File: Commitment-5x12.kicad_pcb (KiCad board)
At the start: 2 copper layers, 234.4 x 118.4 mm, 95 parts, among them J1 Conn_01x13, J2 Conn_01x13, J3 Conn_01x03, J4 Conn_01x04, J5 Conn_01x04, SW1 OS102011MS2QN1, SW2 RotaryEncoder

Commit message: working toward rev 1
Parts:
- added M1: ~, lizard_libs:MX_2U_Stabilizer_Mount, F.Cu at (159.4, 138.4)
- added M2: ~, lizard_libs:MX_2U_Stabilizer_Mount, F.Cu at (121.3, 138.4)
- MX1, MX10, MX11, MX12, MX13, MX14, MX15, MX16, MX17, MX18, MX19, MX2, MX20, MX21, MX22, MX23, MX24, MX26, MX27, MX28, MX29, MX3, MX31, MX32, MX33, MX34, MX36, MX37, MX38, MX39, MX4, MX41, MX42, MX43, MX44, MX45, MX46, MX47, MX48, MX49, MX5, MX50, MX51, MX52, MX53, MX54, MX55, MX56, MX57, MX58, MX59, MX6, MX60, MX7, MX8, MX9: footprint lizard_libs:SW_Cherry_MX_1.00u_PCB -> lizard_libs:hotswap_keyswitch_reflow
- MX25, MX40: footprint lizard_libs:SW_Cherry_MX_2.00u_PCB -> lizard_libs:hotswap_keyswitch_reflow
- moved D1 17.7 mm to (66.0, 63.5)
- moved D13 17.7 mm to (66.0, 120.7)
- moved D9 17.6 mm to (66.0, 101.6)
- moved D3 17.6 mm to (180.3, 63.5)
- moved D17 17.6 mm to (66.0, 139.7)
- moved D5 17.6 mm to (66.0, 82.5)
- moved D2 17.6 mm to (123.2, 63.5)
- moved D15 17.5 mm to (180.3, 120.7)
- moved D14 17.5 mm to (123.2, 120.7)
- moved D11 17.5 mm to (180.3, 101.6)
- moved D10 17.5 mm to (123.2, 101.6)
- moved D7 17.5 mm to (180.3, 82.5)
- moved D6 17.5 mm to (123.2, 82.5)
- moved D19 11.3 mm to (173.7, 135.6)
- moved D18 7.04 mm to (112.1, 135.6)
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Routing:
- net COL 12: track 412.0 -> 334.2 mm, vias 1 -> 8
- net COL 3: track 207.3 -> 148.2 mm, vias 0 -> 7
- net COL 11: track 347.0 -> 288.6 mm, vias 1 -> 7
- net COL 10: track 313.3 -> 255.3 mm, vias 1 -> 7
- net GND: track 100.0 -> 50.7 mm, vias 100 -> 102
- net /BAT +: track 353.9 -> 307.0 mm, vias 8 -> 3
- net COL 8: track 271.3 -> 233.3 mm, vias 1 -> 7
- net COL 4: track 185.5 -> 149.2 mm, vias 1 -> 7
- net COL 9: track 288.8 -> 253.6 mm, vias 2 -> 7
- net COL 5: track 223.3 -> 188.5 mm, vias 1 -> 7
- net ROW 4: track 255.4 -> 272.2 mm
- net ROW 1: track 213.1 -> 228.7 mm
- net Net-(D13A-A): track 6.15 -> 20.9 mm
- net Net-(D1A-A): track 6.19 -> 20.6 mm
- net Net-(D15A-A): track 7.35 -> 20.9 mm
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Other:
- outline, holes or cut-outs redrawn

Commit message: working toward rev 1
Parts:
- moved BAT1 8.89 mm to (190.5, 35.6)
- moved G*** 8.89 mm to (190.5, 35.6)
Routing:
- net Net-(BAT1-+): track 113.7 -> 104.3 mm
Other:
- outline, holes or cut-outs redrawn
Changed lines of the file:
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@@
 		(pad_to_mask_clearance 0)
 		(allow_soldermask_bridges_in_footprints no)
-		(grid_origin 35.56 62.23)
+		(grid_origin 38.1 57.15)
 		(pcbplotparams
 			(layerselection 0x00010fc_ffffffff)
@@
 		(tags "Cherry MX keyswitch 2.00u PCB")
 		(property "Reference" "M1"
-			(at -2.54 -2.794 360)
+			(at -2.54 -2.794 0)
 			(layer "F.SilkS")
 			(hide yes)
@@
 		)
 		(property "Value" "~"
-			(at -2.54 12.954 360)
+			(at -2.54 12.954 0)
 			(layer "F.Fab")
 			(effects
@@
 		)
 		(fp_text user "${REFERENCE}"
-			(at -2.54 -2.794 360)
+			(at -2.54 -2.794 0)
 			(layer "F.Fab")
 			(effects
@@
 	(footprint "lizard_libs:Lizard Text Logo"
 		(layer "F.Cu")
-		(at 199.39 35.56)
+		(at 190.5 35.56)
 		(property "Reference" "G***"
 			(at 0 2.54 0)
@@
 		(tags "Cherry MX keyswitch 2.00u PCB")
 		(property "Reference" "M2"
-			(at -2.54 -2.794 360)
+			(at -2.54 -2.794 0)
 			(layer "F.SilkS")
 			(hide yes)
@@
 		)
 		(property "Value" "~"
-			(at -2.54 12.954 360)
+			(at -2.54 12.954 0)
 			(layer "F.Fab")
 			(effects
@@
 		)
 		(fp_text user "${REFERENCE}"
-			(at -2.54 -2.794 360)
+			(at -2.54 -2.794 0)
 			(layer "F.Fab")
 			(effects
@@
 	(footprint "lizard_libs:Keystone 1043 18650"
 		(layer "F.Cu")
-		(at 199.39 35.56 180)
+		(at 190.5 35.56 180)
 		(property "Reference" "BAT1"
 			(at 0 -2.54 180)
@@
 	)
 	(gr_arc
-		(start 159.766 26.2255)
-		(mid 160.230968 25.102968)
-		(end 161.3535 24.638)
+		(start 149.606 26.2255)
+		(mid 150.070968 25.102968)
+		(end 151.1935 24.638)
 		(stroke
 			(width 0.05)
@@
 	)
 	(gr_line
-		(start 159.766 26.2255)
-		(end 159.766 43.3705)
+		(start 149.606 26.2255)
+		(end 149.606 43.3705)
 		(stroke
 			(width 0.05)
@@
 	)
 	(gr_line
-		(start 158.1785 44.958)
+		(start 148.0185 44.958)
 		(end 81.3435 44.958)
 		(stroke
@@
 	)
 	(gr_arc
-		(start 159.766 43.3705)
-		(mid 159.301032 44.493032)
-		(end 158.1785 44.958)
+		(start 149.606 43.3705)
+		(mid 149.141032 44.493032)
+		(end 148.0185 44.958)
 		(stroke
 			(width 0.05)
@@
 	)
 	(gr_line
-		(start 161.3535 24.638)
+		(start 151.1935 24.638)
 		(end 255.7145 24.638)
 		(stroke
@@
 	)
 	(gr_text "+"
-		(at 172.466 35.433 180)
+		(at 163.576 35.433 180)
 		(layer "F.SilkS")
 		(effects
@@
 	)
 	(gr_text "-"
-		(at 227.711 35.433 180)
+		(at 218.821 35.433 180)
 		(layer "F.SilkS")
 		(effects
@@
 	)
 	(segment
-		(start 70.39 34.83)
-		(end 72.39 36.83)
-		(width 1.27)
-		(layer "F.Cu")
-		(net 1)
-	)
-	(segment
-		(start 163.322 44.45)
-		(end 163.322 35.6235)
+		(start 68.58 34.83)
+		(end 70.39 34.83)
 		(width 1.27)
 		(layer "F.Cu")
@@
 	(segment
 		(start 75.184 46.736)
-		(end 161.036 46.736)
+		(end 151.384 46.736)
 		(width 1.27)
 		(layer "F.Cu")
@@
 	)
 	(segment
-		(start 163.322 35.6235)
-		(end 163.2585 35.56)
+		(start 154.3685 43.7515)
+		(end 154.3685 35.56)
 		(width 1.27)
 		(layer "F.Cu")
@@
 	)
 	(segment
-		(start 68.58 34.83)
-		(end 70.39 34.83)
+		(start 70.39 34.83)
+		(end 72.39 36.83)
 		(width 1.27)
 		(layer "F.Cu")
@@
 	)
 	(segment
-		(start 161.036 46.736)
-		(end 163.322 44.45)
+		(start 151.384 46.736)
+		(end 154.3685 43.7515)
 		(width 1.27)
 		(layer "F.Cu")
@@
 		)
 	)
+	(group ""
+		(members "3122b99c-ad25-44f4-953b-640c3fc964a2" "711c629b-a350-407e-8104-c2bea098a2da"
+			"d03c237c-e164-42e6-be8a-686f8292c659"
+		)
+	)

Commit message: Update Commitment-5x12.kicad_pcb
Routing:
- net Net-(D21-A): track 54.6 -> 55.3 mm
- net GND: vias 102 -> 106
- net (no net): vias 0 -> 1
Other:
- board text added: "JLCJLCJLCJLC"

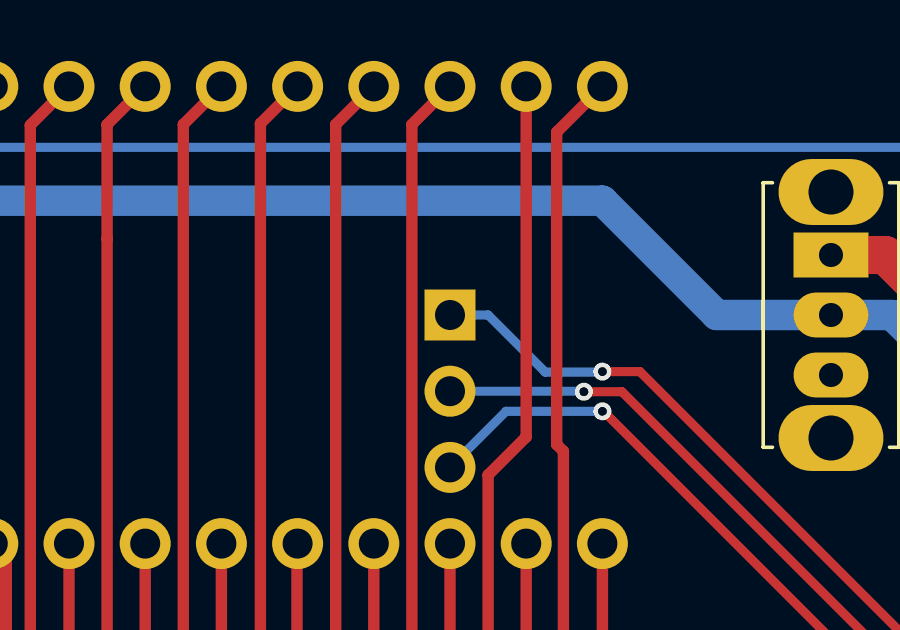
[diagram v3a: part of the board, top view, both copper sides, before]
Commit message: updated footprints to include 3D cad files
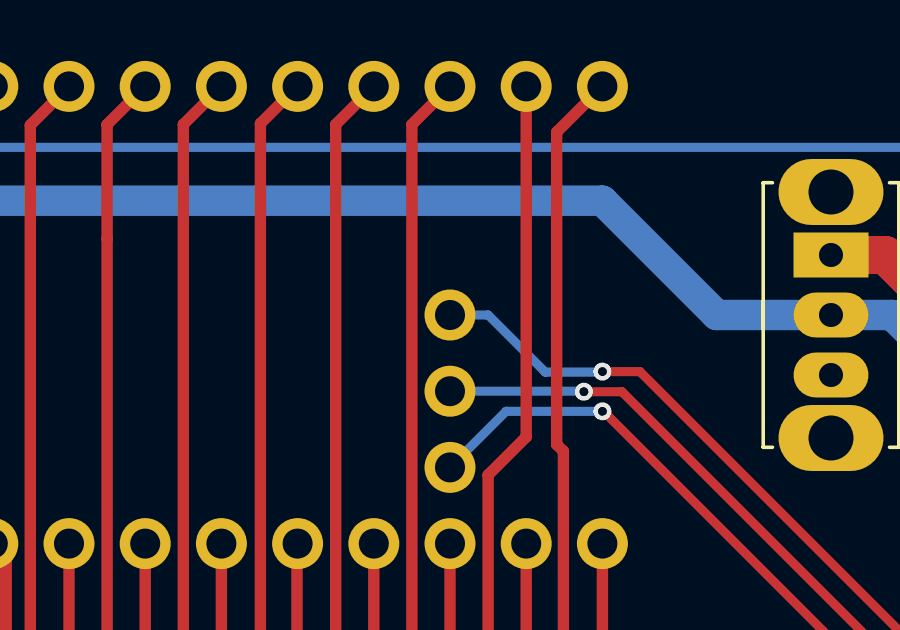
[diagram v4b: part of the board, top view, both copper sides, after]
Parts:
- J3: footprint lizard_libs:PinHeader_1x03_P2.54mm_Vertical -> lizard_libs:PinSocket_1x03_P2.54mm_Vertical
- MX1, MX10, MX11, MX12, MX13, MX14, MX15, MX16, MX17, MX18, MX19, MX2, MX20, MX21, MX22, MX23, MX24, MX25, MX26, MX27, MX28, MX29, MX3, MX31, MX32, MX33, MX34, MX36, MX37, MX38, MX39, MX4, MX40, MX41, MX42, MX43, MX44, MX45, MX46, MX47, MX48, MX49, MX5, MX50, MX51, MX52, MX53, MX54, MX55, MX56, MX57, MX58, MX59, MX6, MX60, MX7, MX8, MX9: footprint lizard_libs:hotswap_keyswitch_reflow -> lizard_libs:Kailh_MX_Hotswap_Socket

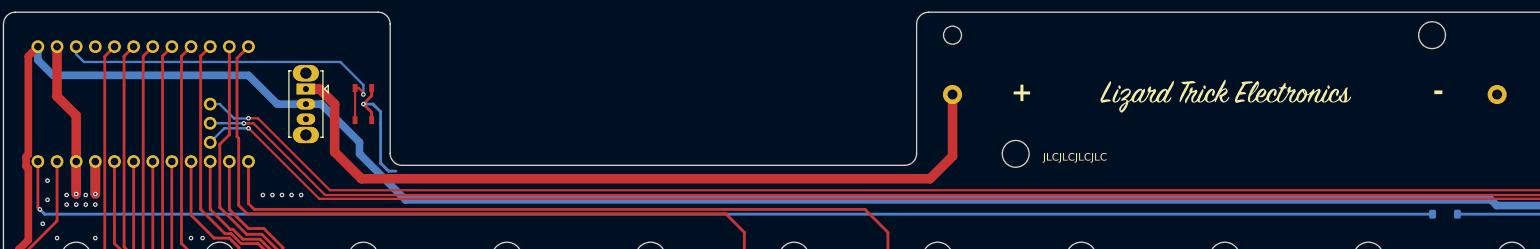
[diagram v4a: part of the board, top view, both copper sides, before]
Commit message: Switched to B3F reset switch
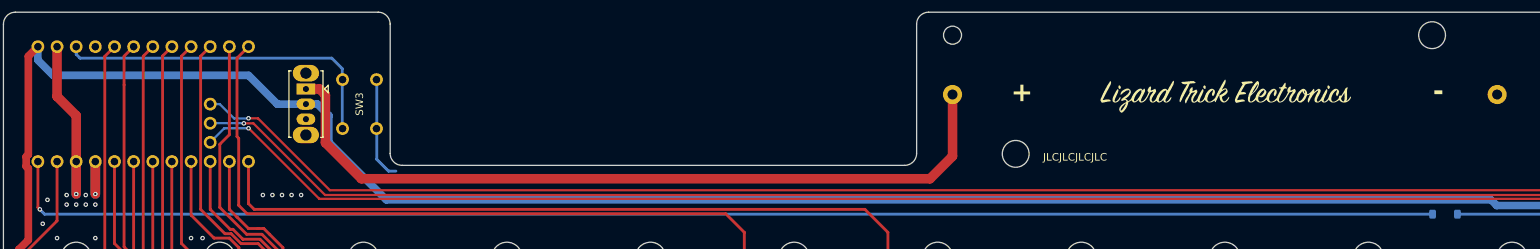
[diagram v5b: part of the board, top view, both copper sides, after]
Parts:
- removed S1: PTS810, lizard_libs:PTS_180_Tactile_Switch
- added SW3: SW_SPST, lizard_libs:Omron_B3F-1000, F.Cu at (75.7, 36.8)
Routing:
- net GND: track 50.7 -> 47.3 mm, vias 106 -> 105
- net Net-(J2-Pin_10): track 47.9 -> 45.1 mm, vias 1 -> 0
- net /BAT +: track 306.7 -> 307.9 mm
- net (no net): vias 1 -> 0
